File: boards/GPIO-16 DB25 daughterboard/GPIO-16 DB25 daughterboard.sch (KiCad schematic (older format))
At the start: 1 part, among them P0 HEADER

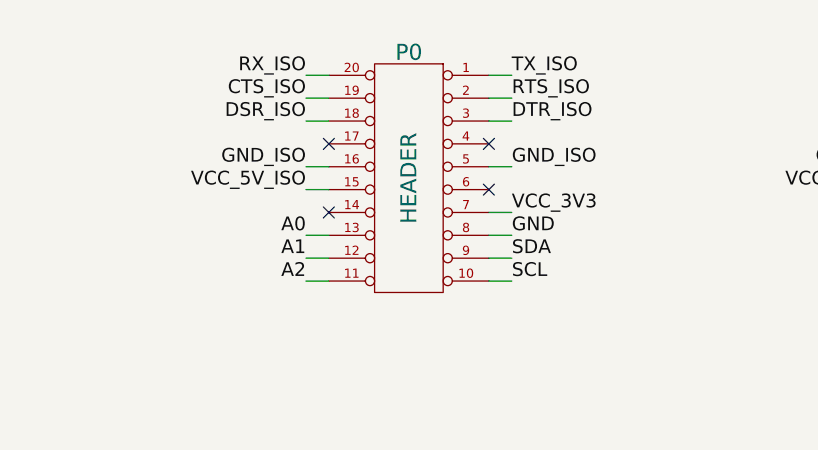
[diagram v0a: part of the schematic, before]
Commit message: Updated daughterboard header pinout in all sheets to be PMOD UART 4/4A compatible
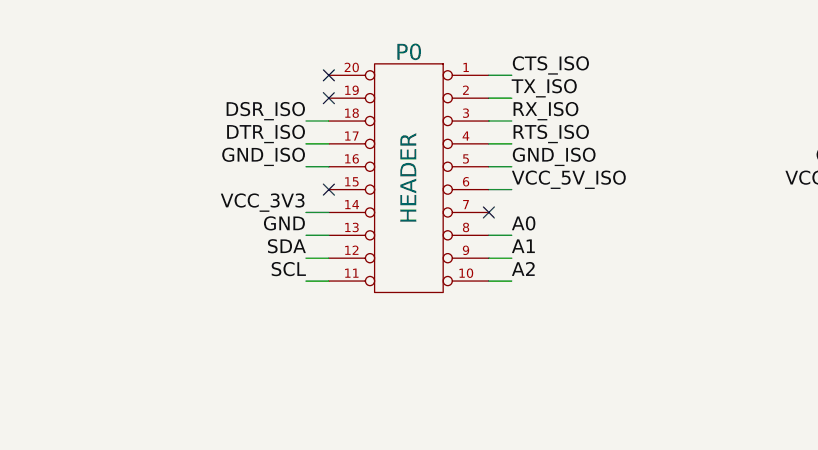
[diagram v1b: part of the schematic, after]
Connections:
- net A0: now also P0.8 (P8); no longer P0.13 (P13)
- net A1: now also P0.9 (P9); no longer P0.12 (P12)
- net A2: now also P0.10 (P10); no longer P0.11 (P11)
- net CTS_ISO: now also P0.1 (P1); no longer P0.19 (P19)
- net DTR_ISO: now also P0.17 (P17); no longer P0.3 (P3)
- net GND: now also P0.13 (P13); no longer P0.8 (P8)
- net RTS_ISO: now also P0.4 (P4); no longer P0.2 (P2)
- net RX_ISO: now also P0.3 (P3); no longer P0.20 (P20)
- net SCL: now also P0.11 (P11); no longer P0.10 (P10)
- net SDA: now also P0.12 (P12); no longer P0.9 (P9)
- net TX_ISO: now also P0.2 (P2); no longer P0.1 (P1)
- net VCC_3V3: now also P0.14 (P14); no longer P0.7 (P7)
- net VCC_5V_ISO: now also P0.6 (P6); no longer P0.15 (P15)
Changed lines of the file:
@@
 Sheet 1 2
 Title ""
-Date "26 jun 2014"
+Date "1 jul 2014"
 Rev ""
 Comp ""
@@
 $EndSheet
 Wire Wire Line
-	3750 3250 3650 3250
+	3750 3450 3650 3450
 Wire Wire Line
-	3750 3350 3650 3350
-Wire Wire Line
-	3750 3450 3650 3450
+	3750 3550 3650 3550
 Wire Wire Line
 	3750 3650 3650 3650
 Wire Wire Line
-	3750 3750 3650 3750
+	4450 3750 4550 3750
 Wire Wire Line
-	3750 3950 3650 3950
+	4450 3950 4550 3950
 Wire Wire Line
 	4550 3250 4450 3250
@@
 	4550 3650 4450 3650
 Wire Wire Line
-	4550 3850 4450 3850
+	3650 3850 3750 3850
 Wire Wire Line
-	4550 3950 4450 3950
+	3650 3950 3750 3950
 Wire Wire Line
-	3750 4050 3650 4050
+	4450 4050 4550 4050
 Wire Wire Line
-	3750 4150 3650 4150
+	4450 4150 4550 4150
 Wire Wire Line
-	4550 4050 4450 4050
+	3650 4050 3750 4050
 Wire Wire Line
-	4550 4150 4450 4150
+	3650 4150 3750 4150
 Text Label 4550 3250 0    60   ~ 0
+CTS_ISO
+Text Label 4550 3350 0    60   ~ 0
 TX_ISO
-Text Label 4550 3350 0    60   ~ 0
-RTS_ISO
 Text Label 4550 3450 0    60   ~ 0
-DTR_ISO
-Text Label 4550 3850 0    60   ~ 0
+RX_ISO
+Text Label 3650 3850 2    60   ~ 0
 VCC_3V3
+Text Label 3650 3950 2    60   ~ 0
+GND
+Text Label 3650 4050 2    60   ~ 0
+SDA
+Text Label 3650 4150 2    60   ~ 0
+SCL
+Text Label 4550 4150 0    60   ~ 0
+A2
+Text Label 4550 4050 0    60   ~ 0
+A1
 Text Label 4550 3950 0    60   ~ 0
-GND
-Text Label 4550 4050 0    60   ~ 0
-SDA
-Text Label 4550 4150 0    60   ~ 0
-SCL
-Text Label 3650 4150 2    60   ~ 0
-A2
-Text Label 3650 4050 2    60   ~ 0
-A1
-Text Label 3650 3950 2    60   ~ 0
 A0
-Text Label 3650 3750 2    60   ~ 0
+Text Label 4550 3750 0    60   ~ 0
 VCC_5V_ISO
 Text Label 3650 3650 2    60   ~ 0
 GND_ISO
+Text Label 3650 3550 2    60   ~ 0
+DTR_ISO
 Text Label 3650 3450 2    60   ~ 0
 DSR_ISO
-Text Label 3650 3350 2    60   ~ 0
-CTS_ISO
-Text Label 3650 3250 2    60   ~ 0
-RX_ISO
 Text Label 4550 3650 0    60   ~ 0
 GND_ISO
-NoConn ~ 4450 3750
-NoConn ~ 4450 3550
-NoConn ~ 3750 3550
-NoConn ~ 3750 3850
 Wire Wire Line
 	6400 3250 6250 3250
@@
 Text Notes 950  7350 0    60   ~ 0
 This sheet abstracts the daughterboard circuits into a hierarchical sheet \nso that they can be integrated into serial expansion motherboard schematic (and PCB) if needed
+Wire Wire Line
+	4450 3550 4550 3550
+Text Label 4550 3550 0    60   ~ 0
+RTS_ISO
+NoConn ~ 3750 3750
+NoConn ~ 4450 3850
+NoConn ~ 3750 3350
+NoConn ~ 3750 3250
 $EndSCHEMATC

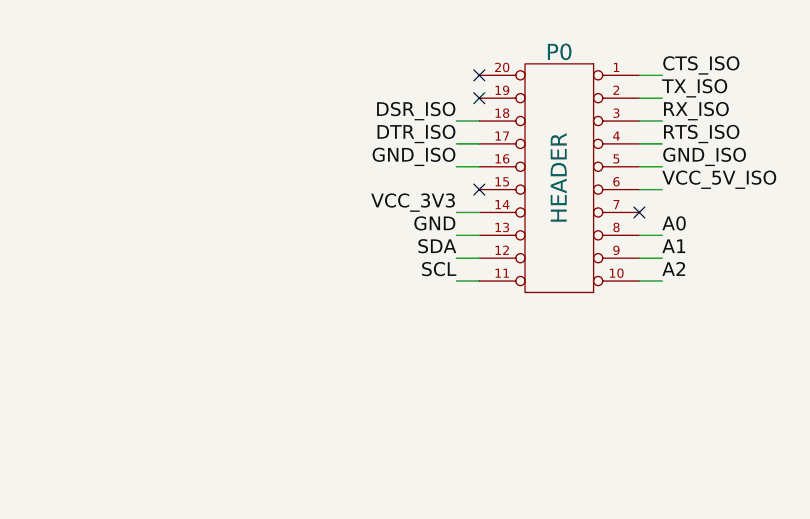
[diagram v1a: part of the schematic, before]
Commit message: Rearranged EEPROM pins in dboard slot pinout to be compatible with PMOD I2C interface
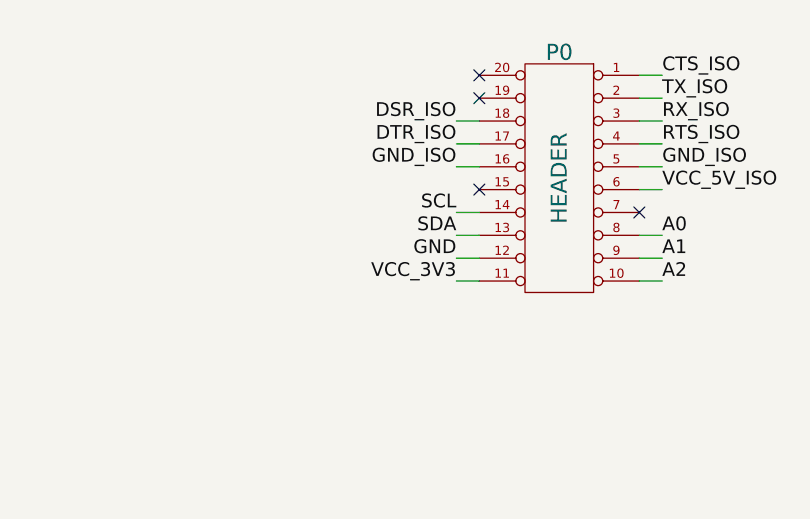
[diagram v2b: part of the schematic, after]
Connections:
- net GND: now also P0.12 (P12); no longer P0.13 (P13)
- net SCL: now also P0.14 (P14); no longer P0.11 (P11)
- net SDA: now also P0.13 (P13); no longer P0.12 (P12)
- net VCC_3V3: now also P0.11 (P11); no longer P0.14 (P14)
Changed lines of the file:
@@
 Sheet 1 2
 Title ""
-Date "1 jul 2014"
+Date "2 jul 2014"
 Rev ""
 Comp ""
@@
 	4550 3650 4450 3650
 Wire Wire Line
-	3650 3850 3750 3850
+	3650 4150 3750 4150
 Wire Wire Line
-	3650 3950 3750 3950
+	3650 4050 3750 4050
 Wire Wire Line
 	4450 4050 4550 4050
@@
 	4450 4150 4550 4150
 Wire Wire Line
-	3650 4050 3750 4050
+	3650 3950 3750 3950
 Wire Wire Line
-	3650 4150 3750 4150
+	3650 3850 3750 3850
 Text Label 4550 3250 0    60   ~ 0
 CTS_ISO
@@
 Text Label 4550 3450 0    60   ~ 0
 RX_ISO
+Text Label 3650 4150 2    60   ~ 0
+VCC_3V3
+Text Label 3650 4050 2    60   ~ 0
+GND
+Text Label 3650 3950 2    60   ~ 0
+SDA
 Text Label 3650 3850 2    60   ~ 0
-VCC_3V3
-Text Label 3650 3950 2    60   ~ 0
-GND
-Text Label 3650 4050 2    60   ~ 0
-SDA
-Text Label 3650 4150 2    60   ~ 0
 SCL
 Text Label 4550 4150 0    60   ~ 0

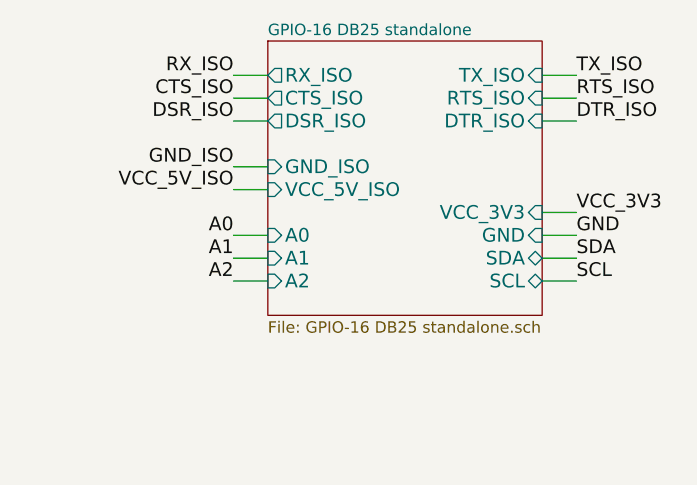
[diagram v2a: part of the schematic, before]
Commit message: Added bypass capacitor to EEPROM in GPIO16 DB25 dboard and cleaned template
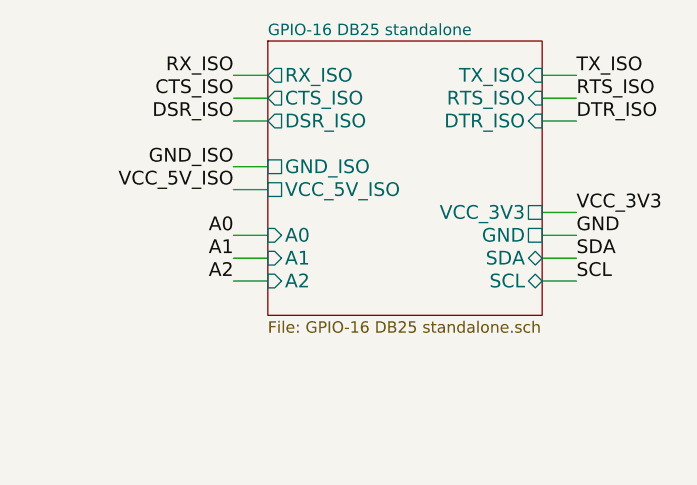
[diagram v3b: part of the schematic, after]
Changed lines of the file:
@@
 Sheet 1 2
 Title ""
-Date "2 jul 2014"
+Date "3 jul 2014"
 Rev ""
 Comp ""
@@
 F6 "DTR_ISO" I R 7600 3450 60
 F7 "DSR_ISO" O L 6400 3450 60
-F8 "VCC_3V3" I R 7600 3850 60
-F9 "GND" I R 7600 3950 60
-F10 "VCC_5V_ISO" I L 6400 3750 60
-F11 "GND_ISO" I L 6400 3650 60
+F8 "VCC_3V3" U R 7600 3850 60
+F9 "GND" U R 7600 3950 60
+F10 "VCC_5V_ISO" U L 6400 3750 60
+F11 "GND_ISO" U L 6400 3650 60
 F12 "SDA" B R 7600 4050 60
 F13 "SCL" B R 7600 4150 60

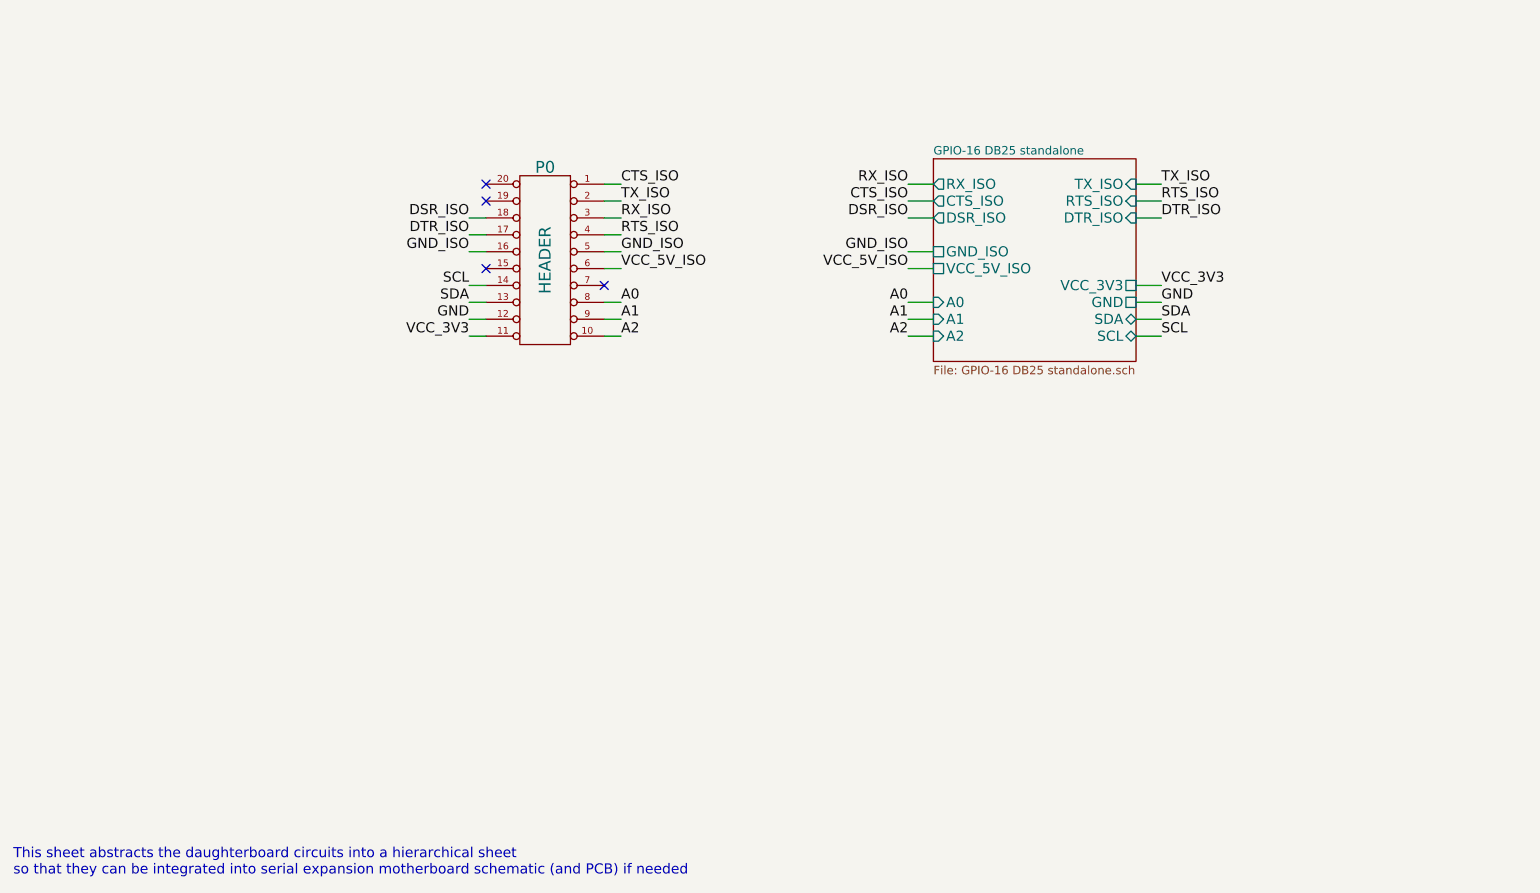
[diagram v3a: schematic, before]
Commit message: GPIO16 DB25 Daughterboard done
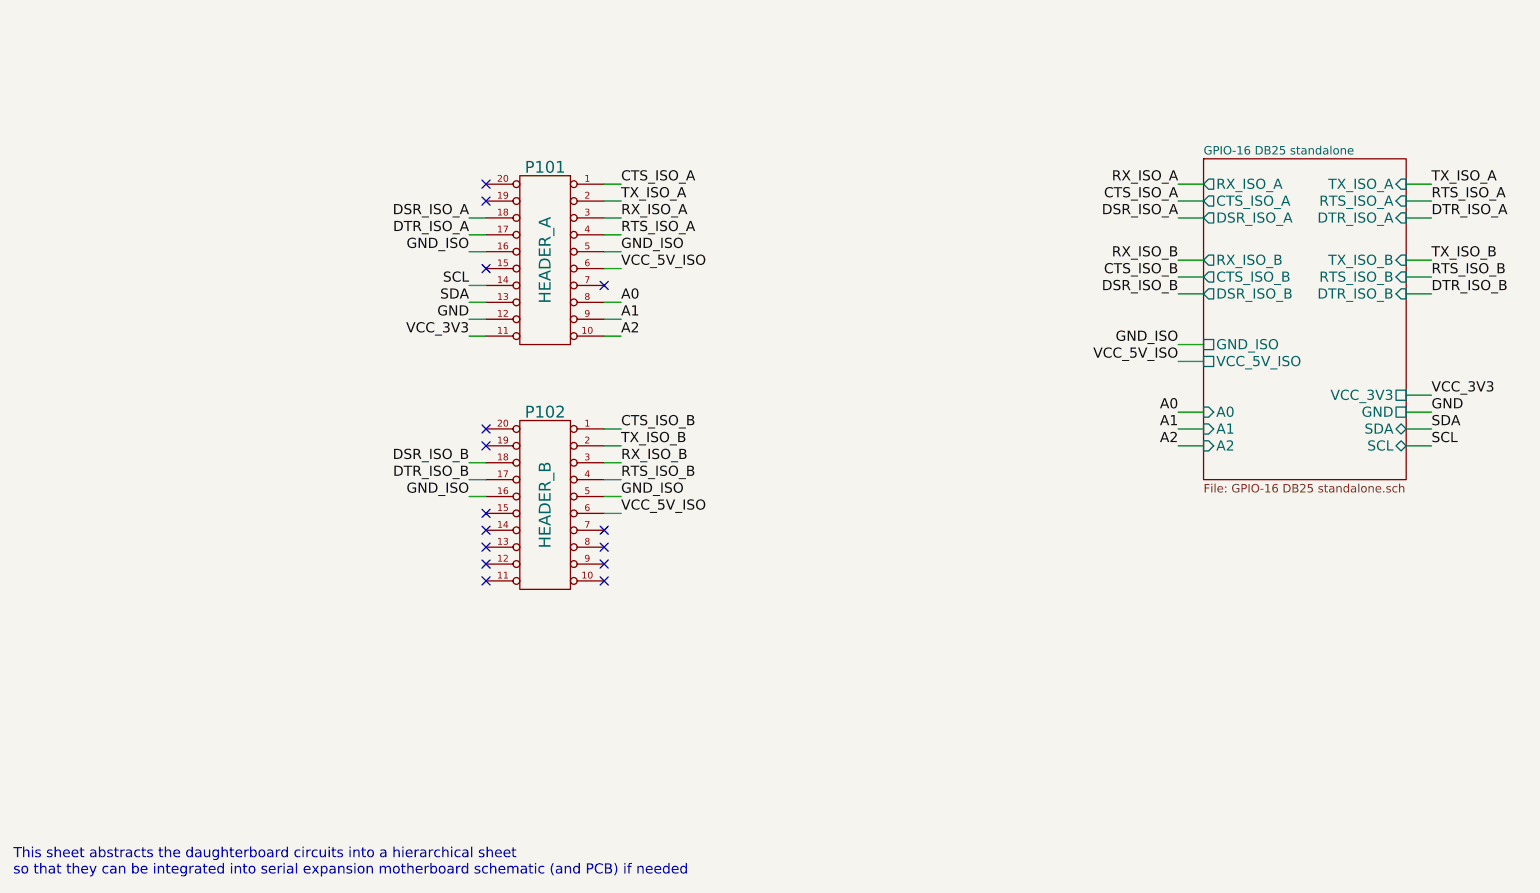
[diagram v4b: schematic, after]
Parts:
- added P102: HEADER_B, symbol DIL20
- P101: renamed from P0; value HEADER -> HEADER_A
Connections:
- net GND_ISO: now also P102.16 (P16), P102.5 (P5)
- net VCC_5V_ISO: now also P102.6 (P6)
- net CTS_ISO renamed CTS_ISO_A
- net DSR_ISO renamed DSR_ISO_A
- net DTR_ISO renamed DTR_ISO_A
- net RTS_ISO renamed RTS_ISO_A
- net RX_ISO renamed RX_ISO_A
- net TX_ISO renamed TX_ISO_A
- new net CTS_ISO_B: P102.1 (P1)
- new net DSR_ISO_B: P102.18 (P18)
- new net DTR_ISO_B: P102.17 (P17)
- new net RTS_ISO_B: P102.4 (P4)
- new net RX_ISO_B: P102.3 (P3)
- new net TX_ISO_B: P102.2 (P2)
- no-connect marks 4 -> 15
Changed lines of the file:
@@
 LIBS:csmall
 LIBS:ISL83387E
+LIBS:pic16f1704
 LIBS:GPIO-16 DB25 daughterboard-cache
 EELAYER 27 0
@@
 $Descr A4 11693 8268
 encoding utf-8
-Sheet 1 2
+Sheet 1 4
 Title ""
 Date "3 jul 2014"
@@
 $EndDescr
 $Comp
-L DIL20 P0
+L DIL20 P101
 U 1 1 53AB69C0
 P 4100 3700
-F 0 "P0" H 4100 4250 70  0000 C CNN
-F 1 "HEADER" V 4100 3700 70  0000 C CNN
+F 0 "P101" H 4100 4250 70  0000 C CNN
+F 1 "HEADER_A" V 4100 3700 70  0000 C CNN
 F 2 "" H 4100 3700 60  0000 C CNN
 F 3 "" H 4100 3700 60  0000 C CNN
@@
 	-1   0    0    -1
 $EndComp
-$Sheet
-S 6400 3100 1200 1200
-U 53AB69CE
-F0 "GPIO-16 DB25 standalone" 50
-F1 "GPIO-16 DB25 standalone.sch" 50
-F2 "TX_ISO" I R 7600 3250 60
-F3 "RX_ISO" O L 6400 3250 60
-F4 "RTS_ISO" I R 7600 3350 60
-F5 "CTS_ISO" O L 6400 3350 60
-F6 "DTR_ISO" I R 7600 3450 60
-F7 "DSR_ISO" O L 6400 3450 60
-F8 "VCC_3V3" U R 7600 3850 60
-F9 "GND" U R 7600 3950 60
-F10 "VCC_5V_ISO" U L 6400 3750 60
-F11 "GND_ISO" U L 6400 3650 60
-F12 "SDA" B R 7600 4050 60
-F13 "SCL" B R 7600 4150 60
-F14 "A0" I L 6400 3950 60
-F15 "A1" I L 6400 4050 60
-F16 "A2" I L 6400 4150 60
-$EndSheet
 Wire Wire Line
 	3750 3450 3650 3450
@@
 	3650 3850 3750 3850
 Text Label 4550 3250 0    60   ~ 0
-CTS_ISO
+CTS_ISO_A
 Text Label 4550 3350 0    60   ~ 0
-TX_ISO
+TX_ISO_A
 Text Label 4550 3450 0    60   ~ 0
-RX_ISO
+RX_ISO_A
 Text Label 3650 4150 2    60   ~ 0
 VCC_3V3
@@
 GND_ISO
 Text Label 3650 3550 2    60   ~ 0
-DTR_ISO
+DTR_ISO_A
 Text Label 3650 3450 2    60   ~ 0
-DSR_ISO
+DSR_ISO_A
 Text Label 4550 3650 0    60   ~ 0
 GND_ISO
 Wire Wire Line
-	6400 3250 6250 3250
-Text Label 6250 3250 2    60   ~ 0
-RX_ISO
-Wire Wire Line
-	6400 3350 6250 3350
-Text Label 6250 3350 2    60   ~ 0
-CTS_ISO
-Wire Wire Line
-	6400 3450 6250 3450
-Text Label 6250 3450 2    60   ~ 0
-DSR_ISO
-Wire Wire Line
-	7750 3250 7600 3250
-Text Label 7750 3250 0    60   ~ 0
-TX_ISO
-Wire Wire Line
-	7750 3350 7600 3350
-Wire Wire Line
-	7750 3450 7600 3450
-Text Label 7750 3350 0    60   ~ 0
-RTS_ISO
-Text Label 7750 3450 0    60   ~ 0
-DTR_ISO
-Wire Wire Line
-	6400 3750 6250 3750
-Text Label 6250 3750 2    60   ~ 0
+	8000 3250 7850 3250
+Text Label 7850 3250 2    60   ~ 0
+RX_ISO_A
+Wire Wire Line
+	8000 3350 7850 3350
+Text Label 7850 3350 2    60   ~ 0
+CTS_ISO_A
+Wire Wire Line
+	8000 3450 7850 3450
+Text Label 7850 3450 2    60   ~ 0
+DSR_ISO_A
+Wire Wire Line
+	9350 3250 9200 3250
+Text Label 9350 3250 0    60   ~ 0
+TX_ISO_A
+Wire Wire Line
+	9350 3350 9200 3350
+Wire Wire Line
+	9350 3450 9200 3450
+Text Label 9350 3350 0    60   ~ 0
+RTS_ISO_A
+Text Label 9350 3450 0    60   ~ 0
+DTR_ISO_A
+Wire Wire Line
+	8000 4300 7850 4300
+Text Label 7850 4300 2    60   ~ 0
 VCC_5V_ISO
 Wire Wire Line
-	6400 3650 6250 3650
-Text Label 6250 3650 2    60   ~ 0
-GND_ISO
-Wire Wire Line
-	6400 3950 6250 3950
-Wire Wire Line
-	6400 4050 6250 4050
-Wire Wire Line
-	6400 4150 6250 4150
-Text Label 6250 4150 2    60   ~ 0
+	8000 4200 7850 4200
+Text Label 7850 4200 2    60   ~ 0
+GND_ISO
+Wire Wire Line
+	8000 4600 7850 4600
+Wire Wire Line
+	8000 4700 7850 4700
+Wire Wire Line
+	8000 4800 7850 4800
+Text Label 7850 4800 2    60   ~ 0
 A2
-Text Label 6250 4050 2    60   ~ 0
+Text Label 7850 4700 2    60   ~ 0
 A1
-Text Label 6250 3950 2    60   ~ 0
+Text Label 7850 4600 2    60   ~ 0
 A0
-Wire Wire Line
-	7750 4050 7600 4050
-Wire Wire Line
-	7750 4150 7600 4150
-Text Label 7750 4050 0    60   ~ 0
+Text Label 9350 4700 0    60   ~ 0
 SDA
-Text Label 7750 4150 0    60   ~ 0
+Text Label 9350 4800 0    60   ~ 0
 SCL
-Wire Wire Line
-	7750 3950 7600 3950
-Text Label 7750 3850 0    60   ~ 0
+Text Label 9350 4500 0    60   ~ 0
 VCC_3V3
-Text Label 7750 3950 0    60   ~ 0
+Text Label 9350 4600 0    60   ~ 0
 GND
-Wire Wire Line
-	7600 3850 7750 3850
-Text Notes 950  7350 0    60   ~ 0
-This sheet abstracts the daughterboard circuits into a hierarchical sheet \nso that they can be integrated into serial expansion motherboard schematic (and PCB) if needed
 Wire Wire Line
 	4450 3550 4550 3550
 Text Label 4550 3550 0    60   ~ 0
-RTS_ISO
+RTS_ISO_A
 NoConn ~ 3750 3750
 NoConn ~ 4450 3850
 NoConn ~ 3750 3350
 NoConn ~ 3750 3250
+Wire Wire Line
+	9350 4500 9200 4500
+Wire Wire Line
+	9200 4600 9350 4600
+Wire Wire Line
+	9350 4700 9200 4700
+Wire Wire Line
+	9200 4800 9350 4800
+Wire Wire Line
+	8000 3700 7850 3700
+Text Label 7850 3700 2    60   ~ 0
+RX_ISO_B
+Wire Wire Line
+	8000 3800 7850 3800
+Text Label 7850 3800 2    60   ~ 0
+CTS_ISO_B
+Wire Wire Line
+	8000 3900 7850 3900
+Text Label 7850 3900 2    60   ~ 0
+DSR_ISO_B
+Text Label 9350 3700 0    60   ~ 0
+TX_ISO_B
+Text Label 9350 3800 0    60   ~ 0
+RTS_ISO_B
+Text Label 9350 3900 0    60   ~ 0
+DTR_ISO_B
+Wire Wire Line
+	9350 3700 9200 3700
+Wire Wire Line
+	9200 3800 9350 3800
+Wire Wire Line
+	9350 3900 9200 3900
+$Comp
+L DIL20 P102
+U 1 1 53B6375B
+P 4100 5150
+F 0 "P102" H 4100 5700 70  0000 C CNN
+F 1 "HEADER_B" V 4100 5150 70  0000 C CNN
+F 2 "" H 4100 5150 60  0000 C CNN
+F 3 "" H 4100 5150 60  0000 C CNN
+	1    4100 5150
+	-1   0    0    -1
+$EndComp
+Wire Wire Line
+	3750 4900 3650 4900
+Wire Wire Line
+	3750 5000 3650 5000
+Wire Wire Line
+	3750 5100 3650 5100
+Wire Wire Line
+	4450 5200 4550 5200
+Wire Wire Line
+	4550 4700 4450 4700
+Wire Wire Line
+	4550 4800 4450 4800
+Wire Wire Line
+	4550 4900 4450 4900
+Wire Wire Line
+	4550 5100 4450 5100
+Text Label 4550 4700 0    60   ~ 0
+CTS_ISO_B
+Text Label 4550 4800 0    60   ~ 0
+TX_ISO_B
+Text Label 4550 4900 0    60   ~ 0
+RX_ISO_B
+Text Label 4550 5200 0    60   ~ 0
+VCC_5V_ISO
+Text Label 3650 5100 2    60   ~ 0
+GND_ISO
+Text Label 3650 5000 2    60   ~ 0
+DTR_ISO_B
+Text Label 3650 4900 2    60   ~ 0
+DSR_ISO_B
+Text Label 4550 5100 0    60   ~ 0
+GND_ISO
+Wire Wire Line
+	4450 5000 4550 5000
+Text Label 4550 5000 0    60   ~ 0
+RTS_ISO_B
+NoConn ~ 3750 5200
+NoConn ~ 4450 5300
+NoConn ~ 3750 4800
+NoConn ~ 3750 4700
+$Sheet
+S 8000 3100 1200 1900
+U 53AB69CE
+F0 "GPIO-16 DB25 standalone" 50
+F1 "GPIO-16 DB25 standalone.sch" 50
+F2 "RX_ISO_A" O L 8000 3250 60
+F3 "RTS_ISO_A" I R 9200 3350 60
+F4 "CTS_ISO_A" O L 8000 3350 60
+F5 "DTR_ISO_A" I R 9200 3450 60
+F6 "DSR_ISO_A" O L 8000 3450 60
+F7 "VCC_3V3" U R 9200 4500 60
+F8 "GND" U R 9200 4600 60
+F9 "VCC_5V_ISO" U L 8000 4300 60
+F10 "GND_ISO" U L 8000 4200 60
+F11 "SDA" B R 9200 4700 60
+F12 "SCL" B R 9200 4800 60
+F13 "A0" I L 8000 4600 60
+F14 "A1" I L 8000 4700 60
+F15 "A2" I L 8000 4800 60
+F16 "TX_ISO_A" I R 9200 3250 60
+F17 "RTS_ISO_B" I R 9200 3800 60
+F18 "CTS_ISO_B" O L 8000 3800 60
+F19 "DTR_ISO_B" I R 9200 3900 60
+F20 "DSR_ISO_B" O L 8000 3900 60
+F21 "TX_ISO_B" I R 9200 3700 60
+F22 "RX_ISO_B" O L 8000 3700 60
+$EndSheet
+Text Notes 950  7350 0    60   ~ 0
+This sheet abstracts the daughterboard circuits into a hierarchical sheet \nso that they can be integrated into serial expansion motherboard schematic (and PCB) if needed
+NoConn ~ 4450 5400
+NoConn ~ 4450 5500
+NoConn ~ 4450 5600
+NoConn ~ 3750 5600
+NoConn ~ 3750 5500
+NoConn ~ 3750 5400
+NoConn ~ 3750 5300
 $EndSCHEMATC
